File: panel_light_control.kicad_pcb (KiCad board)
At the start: 4 copper layers, 90 x 100 mm, 116 parts, among them J1 Conn_01x02, J11 RJ45_Shielded, J13 HR911105A, J2 RJ45_Shielded, J6 Conn_01x04, Q1 IRF540N, Q2 IRF540N, U1 L7805, U2 LM324, U3 STM32F207VGT6, U4 MCP2562-E-P, U5 LAN8720A, Y1 Crystal_GND24

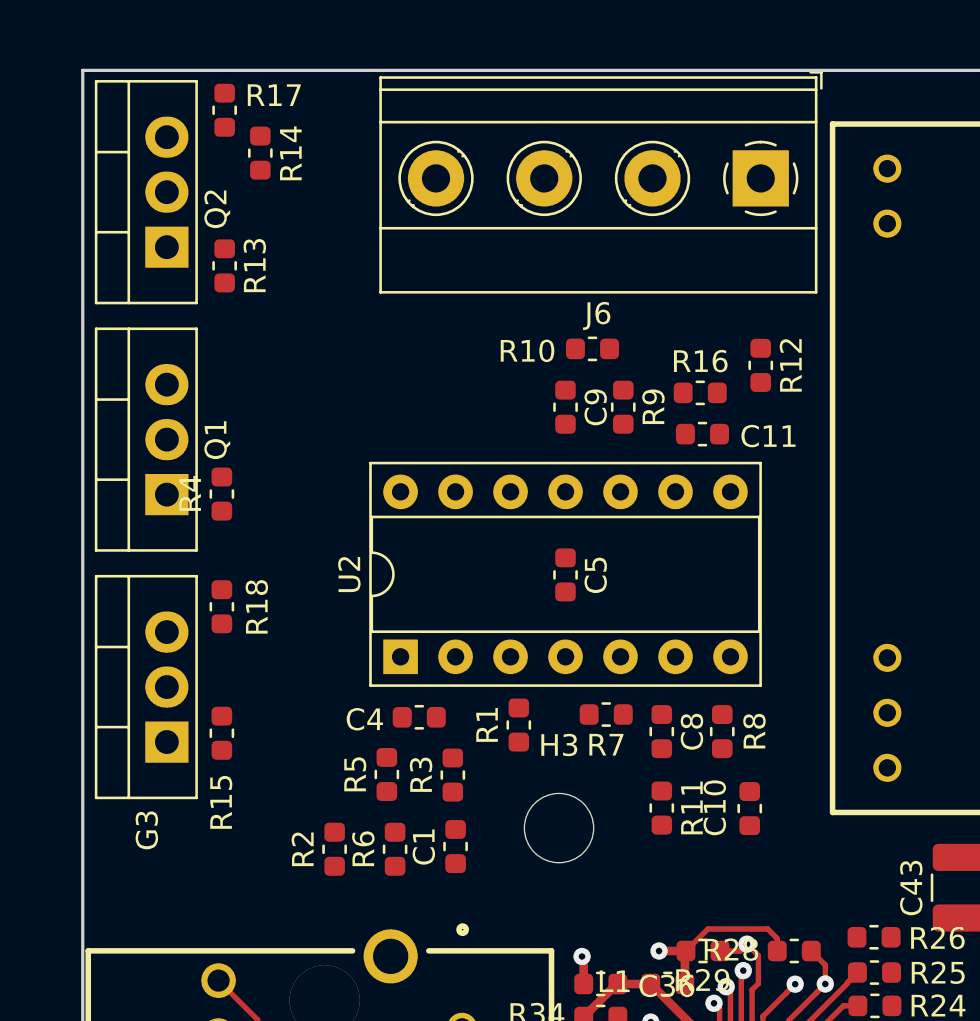
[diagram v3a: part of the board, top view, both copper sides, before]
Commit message: Tweaked MOSFET sink layout. Changed LM324 to SOIC.
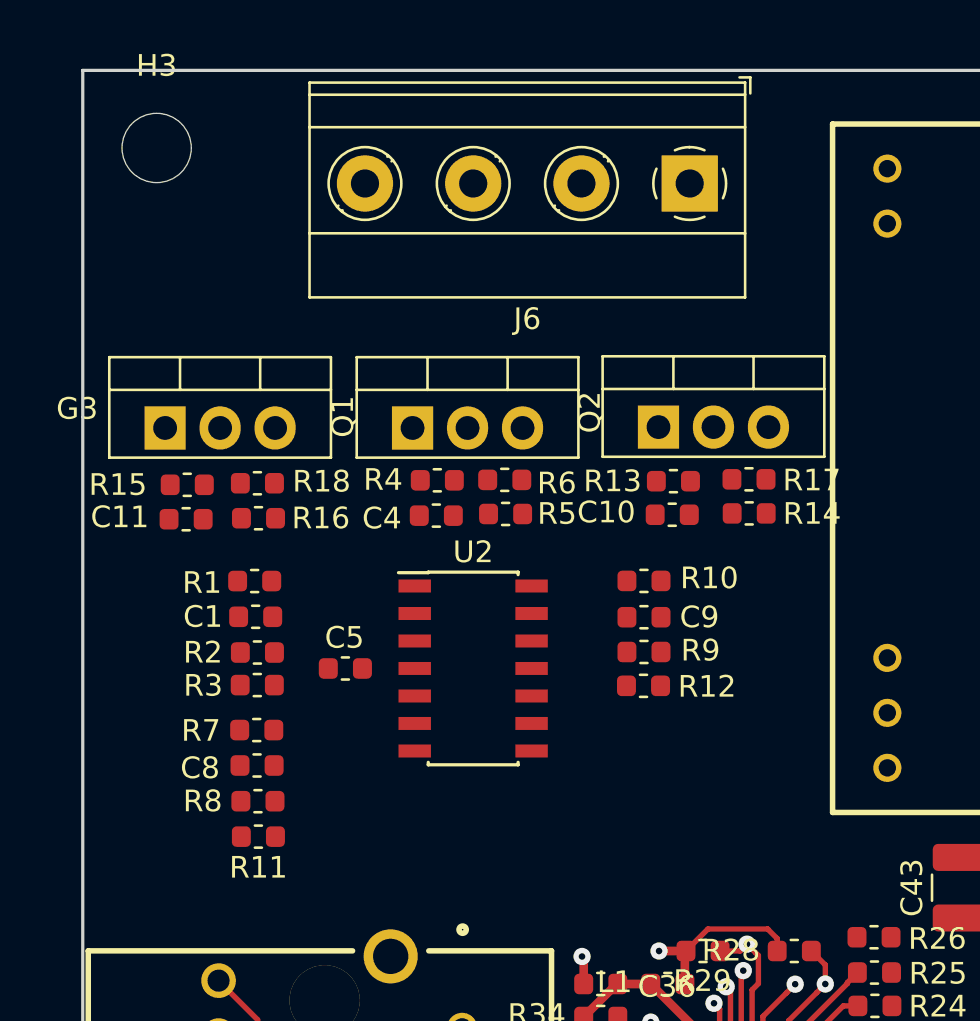
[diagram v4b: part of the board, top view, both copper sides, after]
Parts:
- U2: footprint Package_DIP:DIP-14_W7.62mm_Socket -> Package_SO:SOIC-14_3.9x8.7mm_P1.27mm
- moved H3 36.5 mm to (103.4, 53.6)
- moved R17 29.6 mm to (130.8, 68.9), turned to 0 degrees
- moved R14 28.1 mm to (130.8, 70.5), turned to 0 degrees
- moved Q2 24.2 mm to (126.6, 66.5), turned to 0 degrees
- moved C11 24.2 mm to (104.8, 70.7)
- moved R13 23.0 mm to (127.3, 69.0), turned to 180 degrees
- moved R8 21.7 mm to (108.1, 83.8), turned to 180 degrees
- moved R16 21.2 mm to (108.1, 70.7), turned to 180 degrees
- moved C8 18.8 mm to (108.1, 82.1), turned to 0 degrees
- moved R11 18.7 mm to (108.1, 85.4), turned to 180 degrees
- moved R6 17.8 mm to (119.5, 68.9), turned to 0 degrees
- moved R7 16.2 mm to (108.0, 80.5)
- moved R12 15.8 mm to (125.9, 78.4), turned to 0 degrees
- moved G3 14.5 mm to (103.8, 66.5), turned to 0 degrees
- moved C1 14.1 mm to (108.0, 75.2), turned to 180 degrees
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
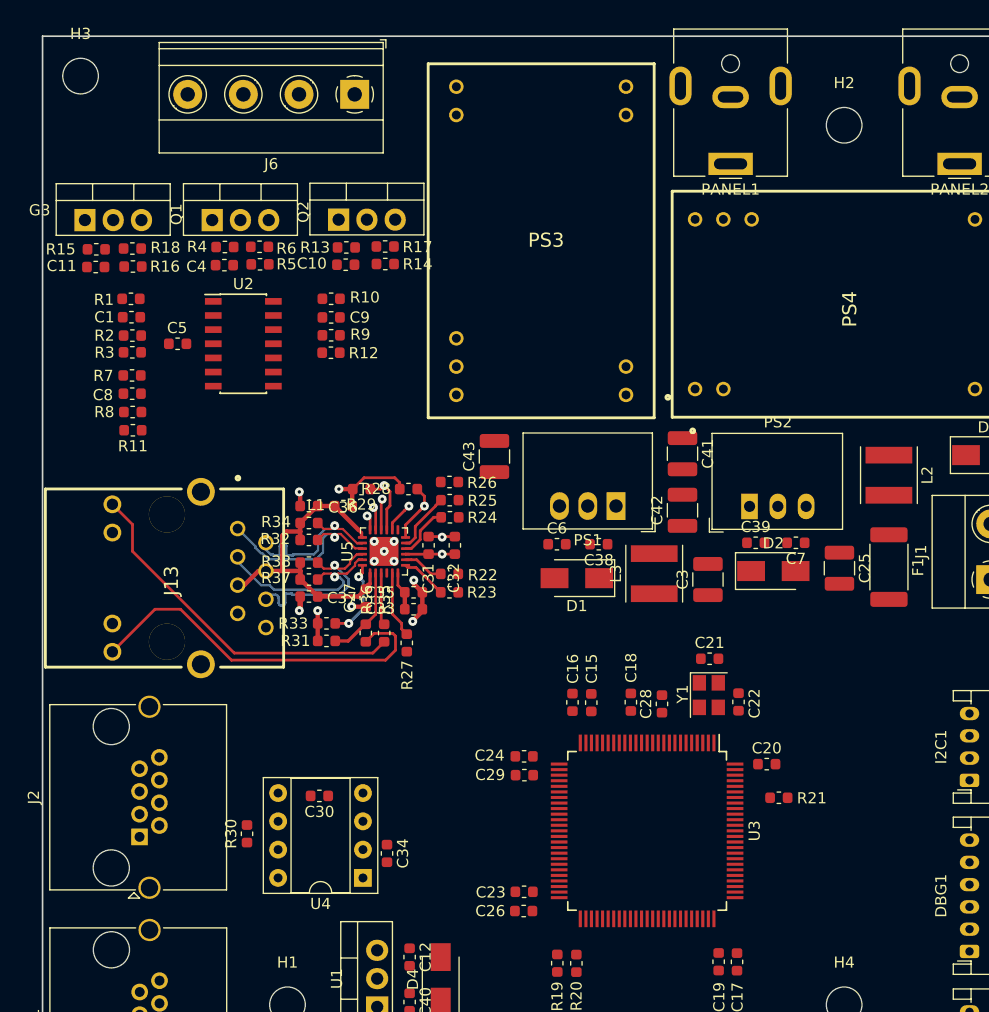
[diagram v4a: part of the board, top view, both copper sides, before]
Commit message: Add LEDs, tweak MOSFET sink.
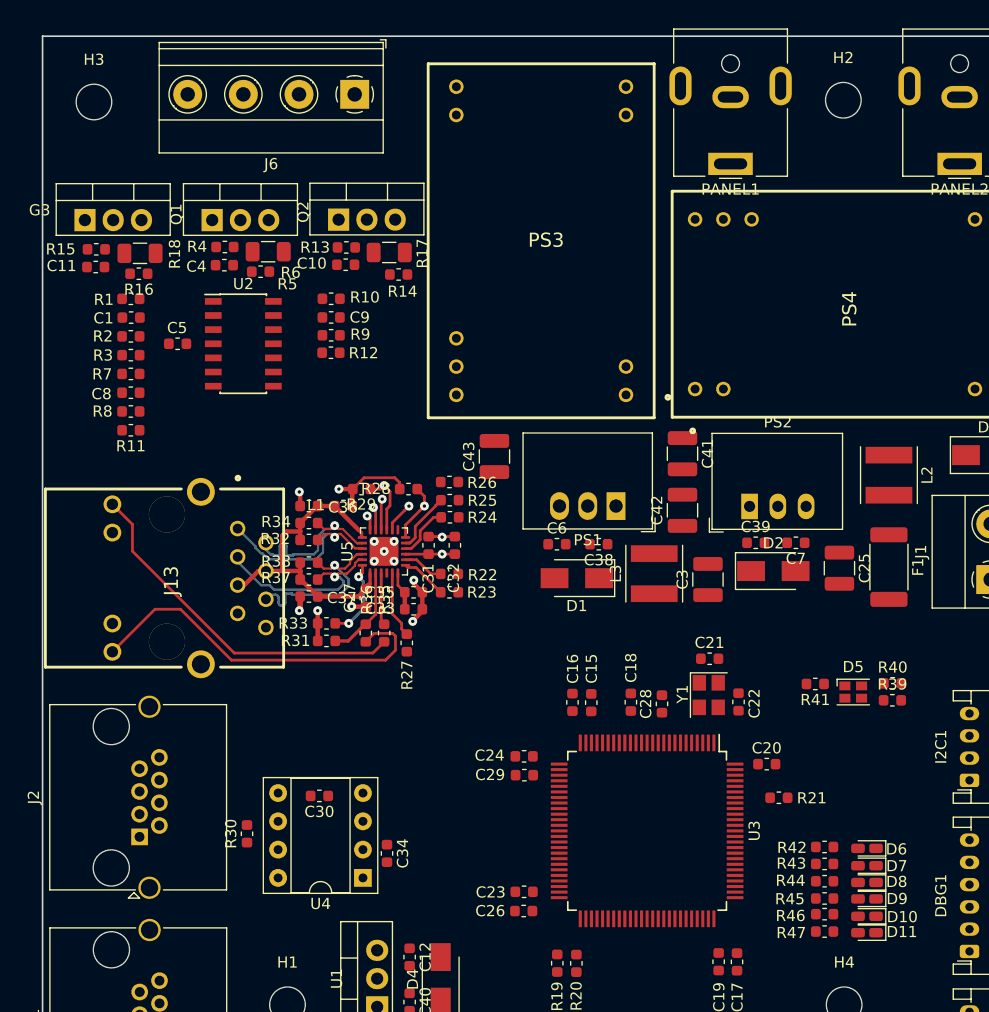
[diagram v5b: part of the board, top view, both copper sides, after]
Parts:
- added D10: LED_WarmWhite, LED_SMD:LED_0603_1608Metric_Castellated, F.Cu at (174.1, 129.1)
- added D11: LED_ColdWhite, LED_SMD:LED_0603_1608Metric_Castellated, F.Cu at (174.1, 130.5)
- added D5: LED_SYSTEM, LED_SMD:LED_Cree-PLCC4_2x2mm_CW, F.Cu at (172.8, 108.9)
- added D6: LED_CAN, LED_SMD:LED_0603_1608Metric_Castellated, F.Cu at (174.1, 123.0)
- added D7: LED_R, LED_SMD:LED_0603_1608Metric_Castellated, F.Cu at (174.1, 124.5)
- added D8: LED_G, LED_SMD:LED_0603_1608Metric_Castellated, F.Cu at (174.1, 126.0)
- added D9: LED_B, LED_SMD:LED_0603_1608Metric_Castellated, F.Cu at (174.1, 127.5)
- added R39: 120R, Resistor_SMD:R_0603_1608Metric, F.Cu at (176.3, 109.7)
- added R40: 120R, Resistor_SMD:R_0603_1608Metric, F.Cu at (176.4, 108.1)
- added R41: 120R, Resistor_SMD:R_0603_1608Metric, F.Cu at (169.4, 108.2)
- added R42: 120R, Resistor_SMD:R_0603_1608Metric, F.Cu at (170.2, 122.8)
- added R43: 120R, Resistor_SMD:R_0603_1608Metric, F.Cu at (170.2, 124.3)
- added R44: 120R, Resistor_SMD:R_0603_1608Metric, F.Cu at (170.2, 125.9)
- added R45: 120R, Resistor_SMD:R_0603_1608Metric, F.Cu at (170.2, 127.5)
- added R46: 120R, Resistor_SMD:R_0603_1608Metric, F.Cu at (170.2, 128.9)
- added R47: 120R, Resistor_SMD:R_0603_1608Metric, F.Cu at (170.2, 130.4)
- R17, R18, R6: footprint Resistor_SMD:R_0603_1608Metric -> Resistor_SMD:R_1206_3216Metric
- moved H3 2.62 mm to (104.6, 55.9)
- moved H2 2.25 mm to (171.9, 55.8)
- moved R14 1.52 mm to (132.0, 71.4)
- moved R6 0.89 mm to (120.3, 69.4)
- moved R16 0.84 mm to (108.6, 71.3)
- moved R18 0.81 mm to (108.8, 69.5)
- moved R5 0.66 mm to (119.6, 71.2)
- moved R17 0.65 mm to (131.1, 69.4)
- moved R3 0.29 mm to (107.9, 78.6)
- moved R11 0.18 mm to (107.9, 85.4)
- moved R7 0.17 mm to (107.9, 80.3)
- moved R8 0.17 mm to (107.9, 83.7)
- moved R2 0.15 mm to (107.9, 77.0)
- moved C8 0.15 mm to (107.9, 82.0)
- turned C1 to 0 degrees
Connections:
- U3 pad 3: Net-(U3-Pad3) -> LED_CW
- U3 pad 38: Net-(U3-Pad38) -> LED_G
- U3 pad 39: Net-(U3-Pad39) -> LED_R
- U3 pad 4: Net-(U3-Pad4) -> LED_WW
- U3 pad 40: Net-(U3-Pad40) -> LED_CAN
- U3 pad 41: Net-(U3-Pad41) -> LED_SYSTEM_B
- U3 pad 42: Net-(U3-Pad42) -> LED_SYSTEM_G
- U3 pad 43: Net-(U3-Pad43) -> LED_SYSTEM_R
- U3 pad 5: Net-(U3-Pad5) -> LED_B

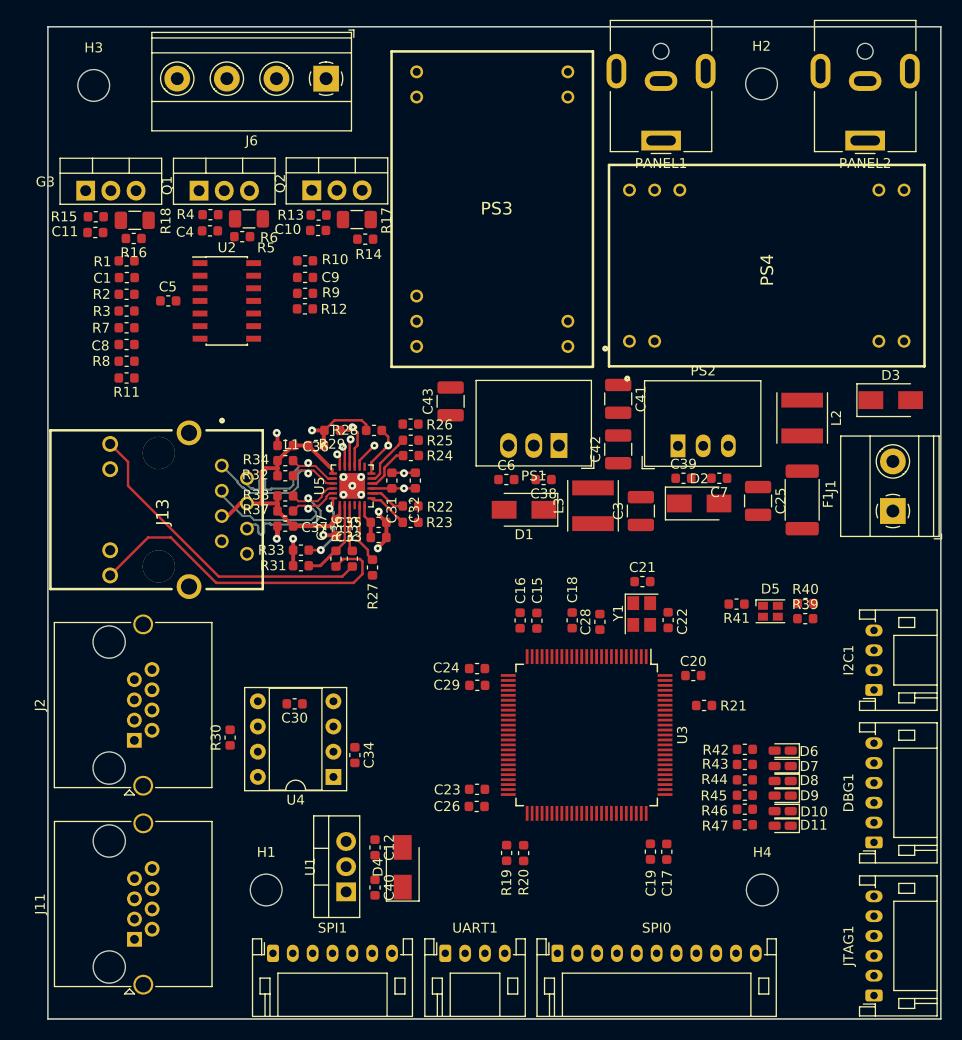
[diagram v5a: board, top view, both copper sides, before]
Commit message: 3.3V buck converter now connected to 12V (prep for 48V>12V upgrade regarding IoP applicability)
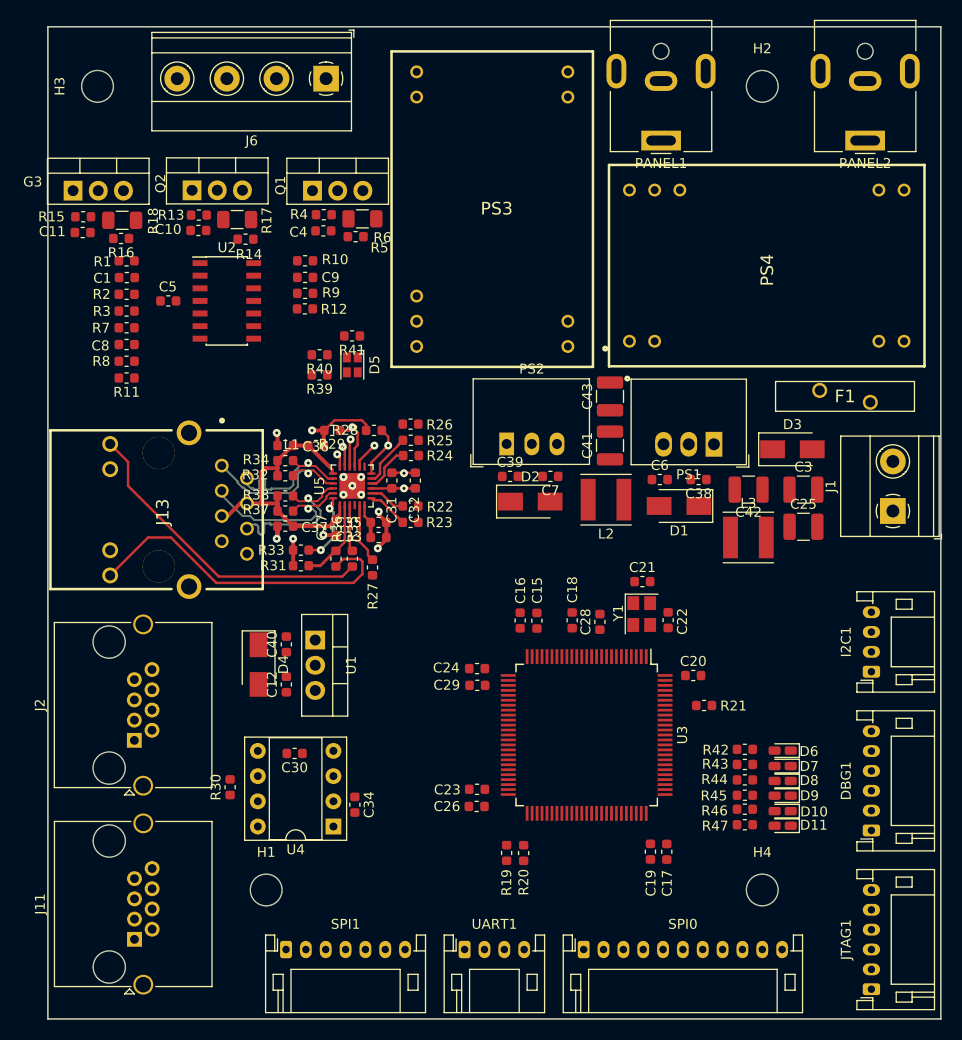
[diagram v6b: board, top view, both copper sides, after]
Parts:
- F1: value Polyfuse_Small -> Polyfuse 3A; footprint Fuse:Fuse_2512_6332Metric -> SamacSys_Parts:30R400UF
- moved R40 55.0 mm to (127.4, 83.1), turned to 180 degrees
- moved R39 54.8 mm to (127.4, 85.1), turned to 180 degrees
- moved D5 48.9 mm to (130.7, 84.1), turned to 270 degrees
- moved R41 47.2 mm to (130.7, 81.2)
- moved C40 26.1 mm to (124.0, 112.2), turned to 90 degrees
- moved U1 25.6 mm to (126.9, 111.8), turned to 270 degrees
- moved D4 25.1 mm to (121.2, 114.3), turned to 270 degrees
- moved L2 21.4 mm to (156.3, 97.7), turned to 180 degrees
- moved C12 18.7 mm to (124.0, 116.3), turned to 90 degrees
- moved C39 17.5 mm to (146.6, 95.3)
- moved PS2 17.3 mm to (146.2, 92.0)
- moved C7 17.0 mm to (150.6, 95.3)
- moved D2 17.0 mm to (148.6, 97.9)
- moved C3 16.5 mm to (176.1, 96.6), turned to 0 degrees
- moved C43 16.1 mm to (156.7, 87.3)
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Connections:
- L2 pad 1: +24V -> +12V
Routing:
- added copper zone on In1.Cu, net GND

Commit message: two sections left to place: 3ch current sink, microcontroller area. Todo: * find proper barrel jacks, spec MPN, Mouser * add status LEDs to the LDD-H outputs * add 7th LED for funsies :> * swap LM324 units around until everything lines up best
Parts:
- R39: value 120R -> 220R
- R40, R41: value 120R -> 1k
- moved D5 5.25 mm to (125.6, 83.0), turned to 0 degrees
- moved R41 5.16 mm to (129.3, 86.1), turned to 0 degrees
- moved C30 4.29 mm to (121.9, 120.1)
- moved R40 2.52 mm to (129.8, 82.3), turned to 0 degrees
- moved R39 2.30 mm to (125.3, 86.1), turned to 0 degrees
- moved L2 0.64 mm to (156.2, 98.3)
- moved PS1 0.53 mm to (167.6, 91.9)
- moved PS2 0.31 mm to (145.9, 92.0)
- moved C41 0.27 mm to (156.7, 92.5)
- moved L3 0.17 mm to (170.4, 101.5), turned to 180 degrees
- moved C43 0.15 mm to (156.7, 87.1)
- moved C42 0.14 mm to (170.6, 96.5)
- renumbered G3 to Q3
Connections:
- R39 pad 2: LED_SYSTEM_B -> PWM_B
- R40 pad 2: LED_SYSTEM_G -> PWM_G
- R41 pad 2: LED_SYSTEM_R -> PWM_R
